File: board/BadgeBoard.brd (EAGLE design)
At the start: 70 x 30 mm, 66 parts

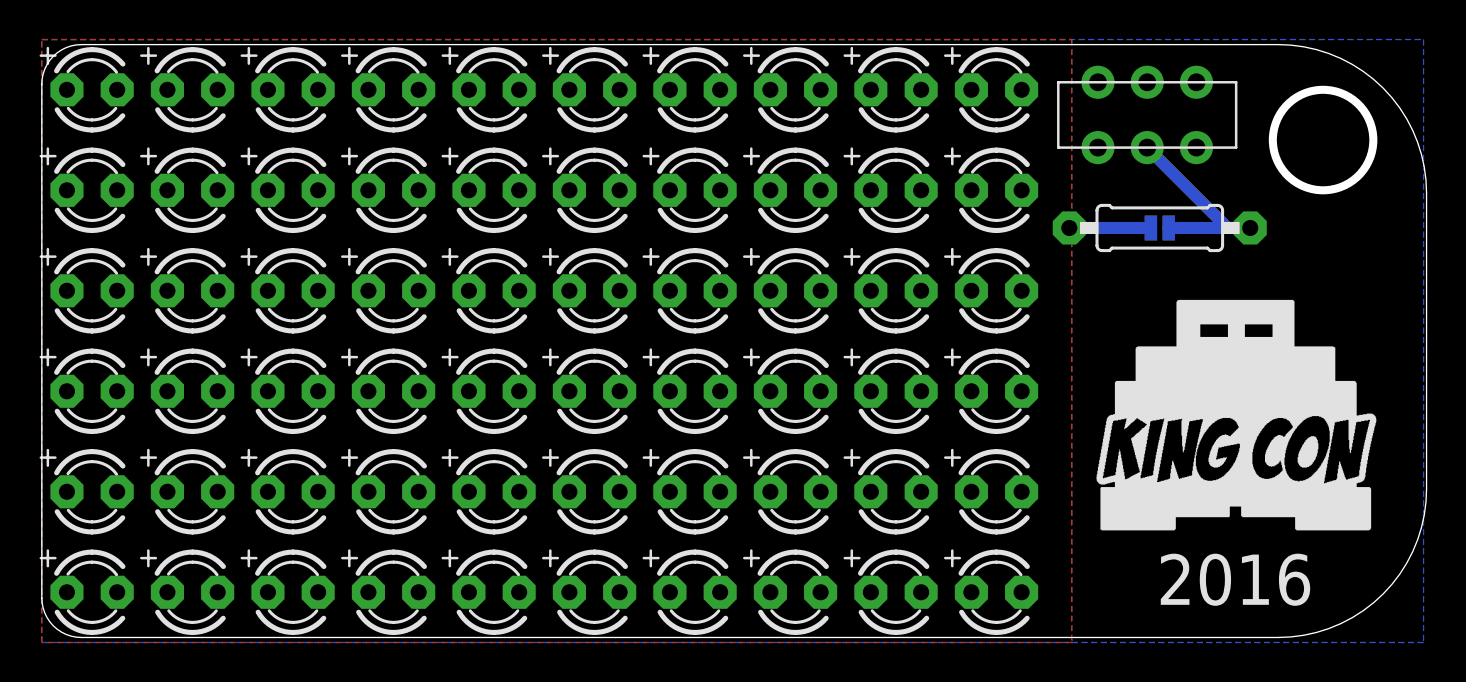
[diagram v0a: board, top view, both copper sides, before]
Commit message: add battery, redo layout a little
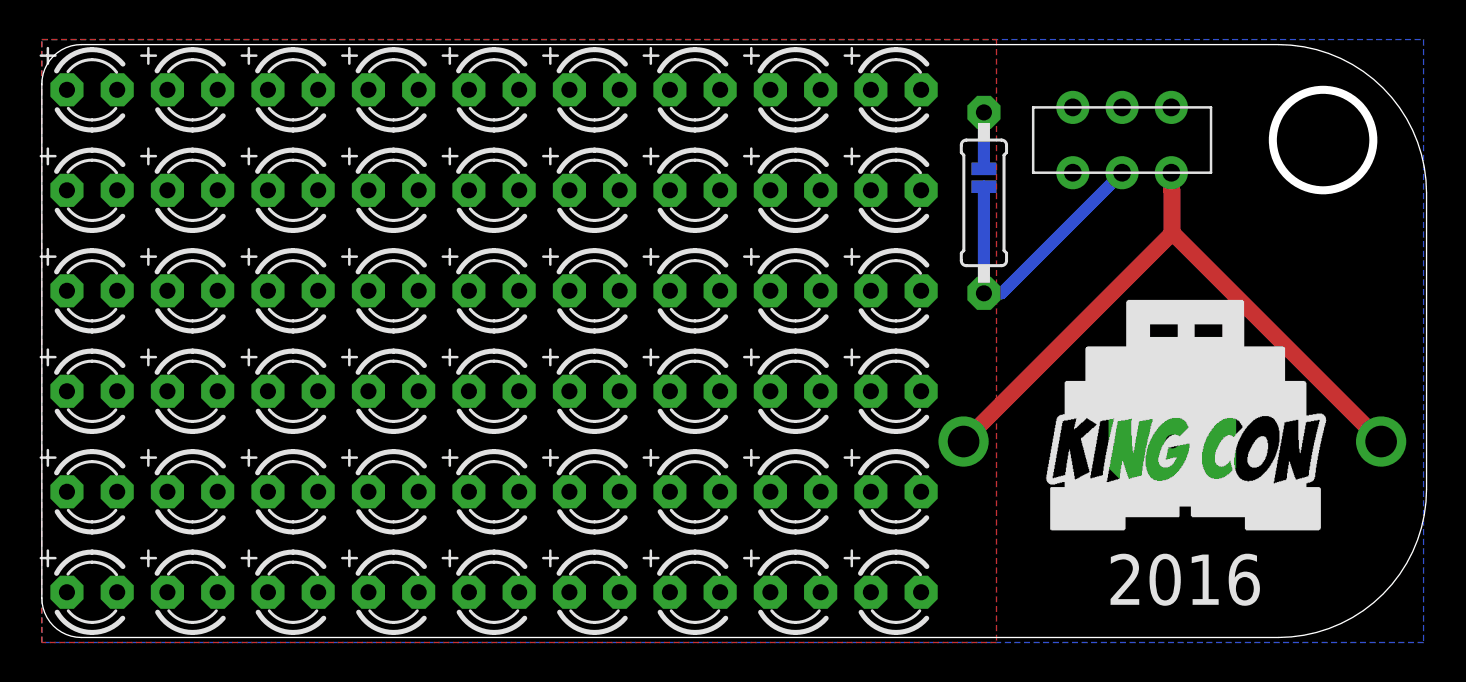
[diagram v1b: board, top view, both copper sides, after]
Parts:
- removed LED55, LED56, LED57, LED58, LED59, LED60: (no value), adafruit:LED3MM
- added U$5: KEYSTONE_3003, battery:KEYSTONE_3003
- moved LED53 25.9 mm to (43.2, 2.54)
- moved JP1 9.25 mm to (47.6, 23.5), turned to 90 degrees
- moved R1 8.98 mm to (47.6, 22.2), turned to 90 degrees
- moved LED52 7.18 mm to (43.2, 7.62)
- moved U$2 3.81 mm to (22.9, 7.62)
- moved U$1 2.54 mm to (50.2, 3.81)
- moved U$3 2.54 mm to (43.2, 5.08)
- moved U$4 1.80 mm to (54.6, 25.4)
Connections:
- net GND: now also U$5.P$3; no longer LED55.K, LED56.K, LED57.K, LED58.K, LED59.K, LED60.K
- net VBATT: now also U$5.P$1, U$5.P$2
- net VLED: no longer LED55.A, LED56.A, LED57.A, LED58.A, LED59.A, LED60.A
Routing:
- net VBATT: track 0.00 -> 35.9 mm
- net SW_BATT: track 11.0 -> 14.9 mm
- net VLED: track 4.12 -> 2.85 mm
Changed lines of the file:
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@@
 <wire x1="70" y1="22.726" x2="62.5" y2="30.226" width="0" layer="20" curve="90"/>
 <circle x="64.77" y="25.4" radius="2.54" width="0.4064" layer="20"/>
-<text x="60.325" y="3.175" size="2.54" layer="25" font="vector" align="center">2016</text>
+<text x="57.785" y="3.175" size="2.54" layer="25" font="vector" align="center">2016</text>
 <text x="26.67" y="25.4" size="3.81" layer="26" rot="MR0" align="center">KingCon 2016</text>
-<text x="38.1" y="5.08" size="1.27" layer="26" font="vector" rot="MR0" align="center">www.kingcon.co.uk</text>
-<text x="17.145" y="5.08" size="1.27" layer="26" font="vector" rot="MR0" align="center">www.makerspace.org.uk</text>
+<text x="35.56" y="5.08" size="1.27" layer="26" font="vector" rot="MR0" align="center">www.kingcon.co.uk</text>
+<text x="13.335" y="5.08" size="1.27" layer="26" font="vector" rot="MR0" align="center">www.makerspace.org.uk</text>
 </plain>
 <attributes>
@@
 <attribute name="VALUE" x="45.085" y="16.129" size="1.27" layer="27" ratio="10"/>
 </element>
-<element name="LED52" library="adafruit" package="LED3MM" value="" x="48.26" y="12.7" smashed="yes">
-<attribute name="VALUE" x="50.165" y="11.049" size="1.27" layer="27" ratio="10"/>
-</element>
-<element name="LED53" library="adafruit" package="LED3MM" value="" x="48.26" y="27.94" smashed="yes">
-<attribute name="VALUE" x="50.165" y="26.289" size="1.27" layer="27" ratio="10"/>
+<element name="LED52" library="adafruit" package="LED3MM" value="" x="43.18" y="7.62" smashed="yes">
+<attribute name="VALUE" x="45.085" y="5.969" size="1.27" layer="27" ratio="10"/>
+</element>
+<element name="LED53" library="adafruit" package="LED3MM" value="" x="43.18" y="2.54" smashed="yes">
+<attribute name="VALUE" x="45.085" y="0.889" size="1.27" layer="27" ratio="10"/>
 </element>
 <element name="LED54" library="adafruit" package="LED3MM" value="" x="43.18" y="12.7" smashed="yes">
 <attribute name="VALUE" x="45.085" y="11.049" size="1.27" layer="27" ratio="10"/>
 </element>
-<element name="LED55" library="adafruit" package="LED3MM" value="" x="48.26" y="7.62" smashed="yes">
-<attribute name="VALUE" x="50.165" y="5.969" size="1.27" layer="27" ratio="10"/>
-</element>
-<element name="LED56" library="adafruit" package="LED3MM" value="" x="48.26" y="22.86" smashed="yes">
-<attribute name="VALUE" x="50.165" y="21.209" size="1.27" layer="27" ratio="10"/>
-</element>
-<element name="LED57" library="adafruit" package="LED3MM" value="" x="43.18" y="7.62" smashed="yes">
-<attribute name="VALUE" x="45.085" y="5.969" size="1.27" layer="27" ratio="10"/>
-</element>
-<element name="LED58" library="adafruit" package="LED3MM" value="" x="48.26" y="2.54" smashed="yes">
-<attribute name="VALUE" x="50.165" y="0.889" size="1.27" layer="27" ratio="10"/>
-</element>
-<element name="LED59" library="adafruit" package="LED3MM" value="" x="48.26" y="17.78" smashed="yes">
-<attribute name="VALUE" x="50.165" y="16.129" size="1.27" layer="27" ratio="10"/>
-</element>
-<element name="LED60" library="adafruit" package="LED3MM" value="" x="43.18" y="2.54" smashed="yes">
-<attribute name="VALUE" x="45.085" y="0.889" size="1.27" layer="27" ratio="10"/>
-</element>
-<element name="U$1" library="KingCon_Logo" package="KINGCON_LOGO_L" value="" x="52.705" y="3.81"/>
-<element name="U$2" library="logos" package="MAKERSPACE_LOGO_FULL_M" value="" x="26.67" y="7.62" rot="MR0"/>
-<element name="U$3" library="logos" package="KINGCON_LOGO_L" value="" x="45.72" y="5.08" rot="MR0"/>
-<element name="U$4" library="switch" package="JS202011CQN" value="JS202011CQN" x="55.88" y="26.67" smashed="yes"/>
-<element name="R1" library="adafruit" package="0207/9" value="" x="56.515" y="20.955" smashed="yes" rot="R180">
-<attribute name="VALUE" x="58.7756" y="21.59" size="1.27" layer="27" ratio="10" rot="R180"/>
-</element>
-<element name="JP1" library="SparkFun-Passives" package="PAD-JUMPER-2-NO_NO_SILK" value="JUMPER-PAD-2-NO" x="56.515" y="20.955" smashed="yes" rot="MR0"/>
+<element name="U$1" library="KingCon_Logo" package="KINGCON_LOGO_L" value="" x="50.165" y="3.81"/>
+<element name="U$2" library="logos" package="MAKERSPACE_LOGO_FULL_M" value="" x="22.86" y="7.62" rot="MR0"/>
+<element name="U$3" library="logos" package="KINGCON_LOGO_L" value="" x="43.18" y="5.08" rot="MR0"/>
+<element name="U$4" library="switch" package="JS202011CQN" value="JS202011CQN" x="54.61" y="25.4" smashed="yes"/>
+<element name="R1" library="adafruit" package="0207/9" value="" x="47.625" y="22.225" smashed="yes" rot="R90">
+<attribute name="VALUE" x="48.26" y="19.9644" size="1.27" layer="27" ratio="10" rot="R90"/>
+</element>
+<element name="JP1" library="SparkFun-Passives" package="PAD-JUMPER-2-NO_NO_SILK" value="JUMPER-PAD-2-NO" x="47.625" y="23.495" smashed="yes" rot="MR90"/>
+<element name="U$5" library="battery" package="KEYSTONE_3003" value="KEYSTONE_3003" x="57.15" y="10.16" smashed="yes" rot="MR180"/>
 </elements>
 <signals>
@@
 <polygon width="0.6096" layer="1">
 <vertex x="0" y="30.48"/>
-<vertex x="52.07" y="30.48"/>
-<vertex x="52.07" y="0"/>
+<vertex x="48.26" y="30.48"/>
+<vertex x="48.26" y="0"/>
 <vertex x="0" y="0"/>
 </polygon>
@@
 <contactref element="LED50" pad="A"/>
 <contactref element="LED49" pad="A"/>
-<contactref element="LED55" pad="A"/>
-<contactref element="LED56" pad="A"/>
-<contactref element="LED57" pad="A"/>
-<contactref element="LED58" pad="A"/>
-<contactref element="LED59" pad="A"/>
-<contactref element="LED60" pad="A"/>
 <contactref element="R1" pad="2"/>
 <contactref element="JP1" pad="2"/>
-<wire x1="56.065" y1="20.955" x2="51.943" y2="20.955" width="0.6096" layer="16"/>
+<wire x1="47.625" y1="23.945" x2="47.625" y2="26.797" width="0.6096" layer="16"/>
 <wire x1="1.27" y1="22.86" x2="1.27" y2="27.94" width="0" layer="19" extent="1-1"/>
 <wire x1="1.27" y1="17.78" x2="1.27" y2="22.86" width="0" layer="19" extent="1-1"/>
@@
 <contactref element="LED8" pad="K"/>
 <contactref element="LED9" pad="K"/>
-<polygon width="0.4064" layer="16">
+<polygon width="0.6096" layer="16">
 <vertex x="0" y="30.48"/>
 <vertex x="69.85" y="30.48"/>
@@
 <contactref element="LED50" pad="K"/>
 <contactref element="LED49" pad="K"/>
-<contactref element="LED55" pad="K"/>
-<contactref element="LED56" pad="K"/>
-<contactref element="LED57" pad="K"/>
-<contactref element="LED58" pad="K"/>
-<contactref element="LED59" pad="K"/>
-<contactref element="LED60" pad="K"/>
+<contactref element="U$5" pad="P$3"/>
 </signal>
 <signal name="SW_BATT">
@@
 <contactref element="R1" pad="1"/>
 <contactref element="JP1" pad="1"/>
-<wire x1="61.087" y1="20.955" x2="56.965" y2="20.955" width="0.6096" layer="16"/>
-<wire x1="55.88" y1="25.019" x2="59.944" y2="20.955" width="0.6096" layer="16"/>
-<wire x1="59.944" y1="20.955" x2="61.087" y2="20.955" width="0.6096" layer="16"/>
+<wire x1="47.625" y1="23.045" x2="47.625" y2="17.653" width="0.6096" layer="16"/>
+<wire x1="54.61" y1="23.749" x2="48.514" y2="17.653" width="0.6096" layer="16"/>
+<wire x1="48.514" y1="17.653" x2="47.625" y2="17.653" width="0.6096" layer="16"/>
 </signal>
 <signal name="VBATT">
 <contactref element="U$4" pad="3"/>
+<contactref element="U$5" pad="P$1"/>
+<contactref element="U$5" pad="P$2"/>
+<wire x1="46.5963" y1="10.16" x2="57.0992" y2="20.6629" width="0.8128" layer="1"/>
+<wire x1="57.0992" y1="20.6629" x2="57.0992" y2="23.749" width="0.8128" layer="1"/>
+<wire x1="67.7037" y1="10.16" x2="57.15" y2="20.7137" width="0.8128" layer="1"/>
+<wire x1="57.15" y1="20.7137" x2="57.15" y2="22.86" width="0.8128" layer="1"/>
+<wire x1="57.15" y1="22.86" x2="57.0992" y2="22.9108" width="0.8128" layer="1"/>
+<wire x1="57.0992" y1="22.9108" x2="57.0992" y2="23.749" width="0.8128" layer="1"/>
 </signal>
 </signals>
